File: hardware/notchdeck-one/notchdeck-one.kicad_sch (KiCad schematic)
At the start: 0 parts

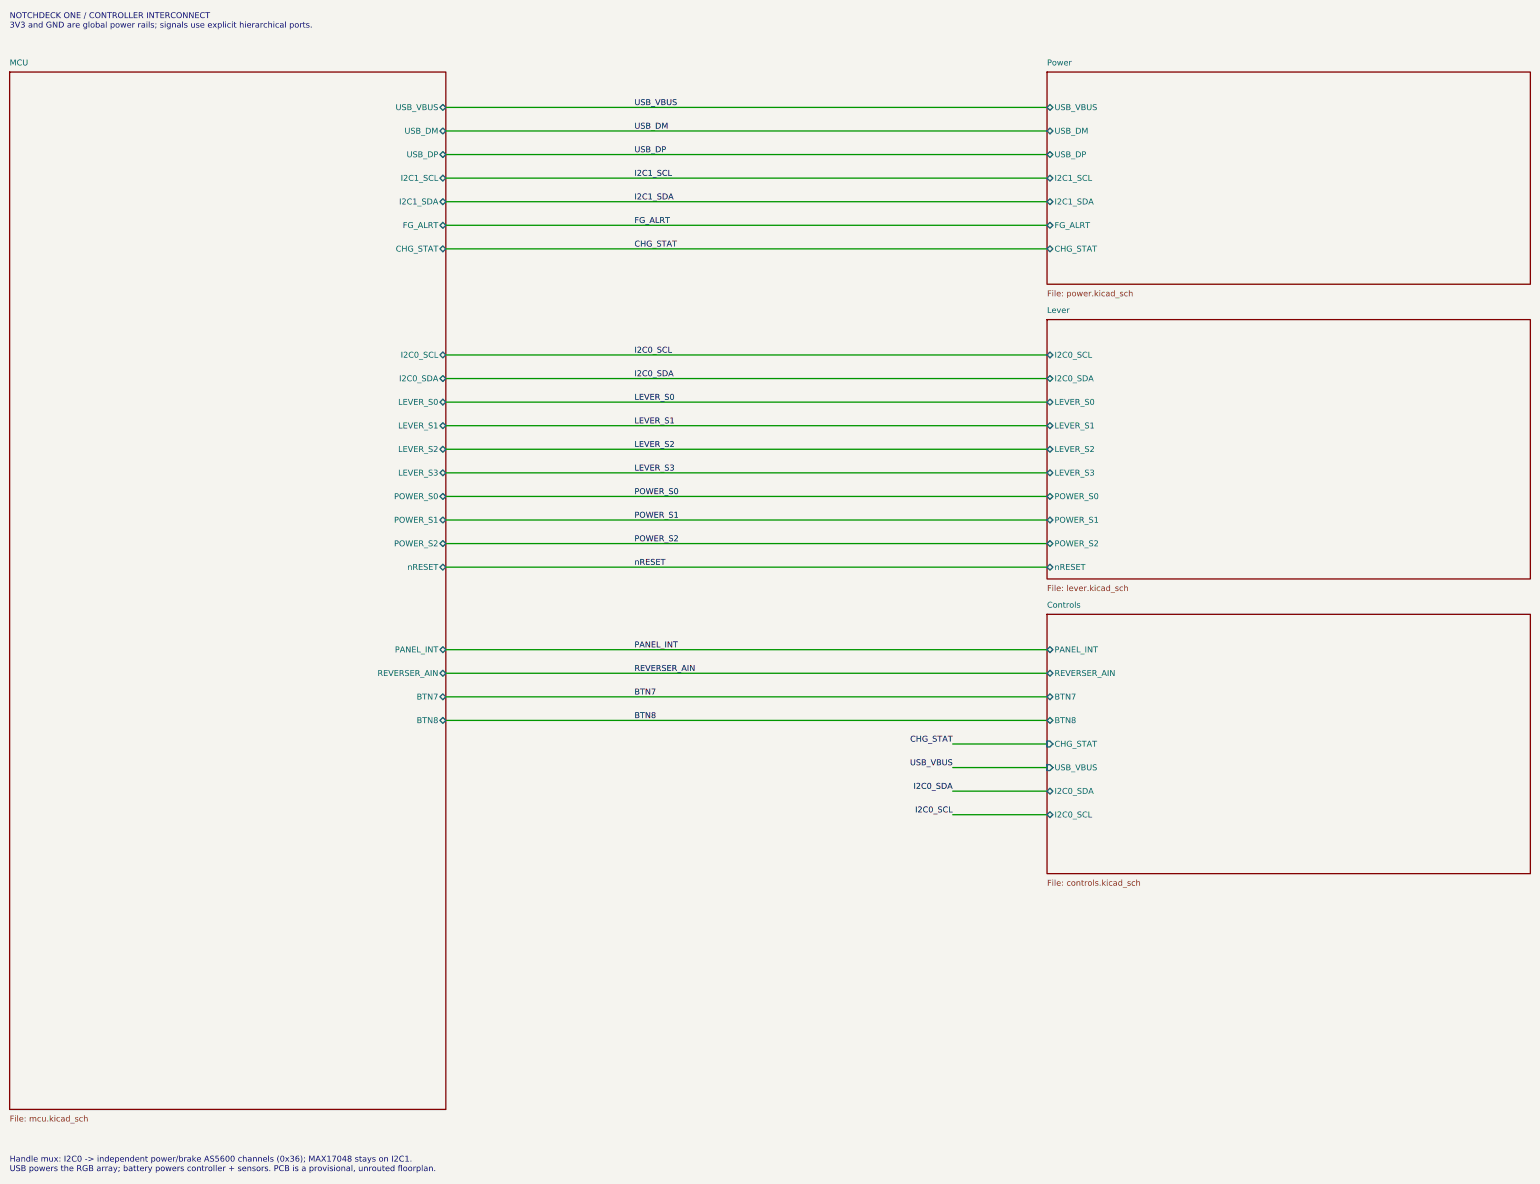
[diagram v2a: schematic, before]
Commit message: Add protected PWM actuator outputs and charger interlock
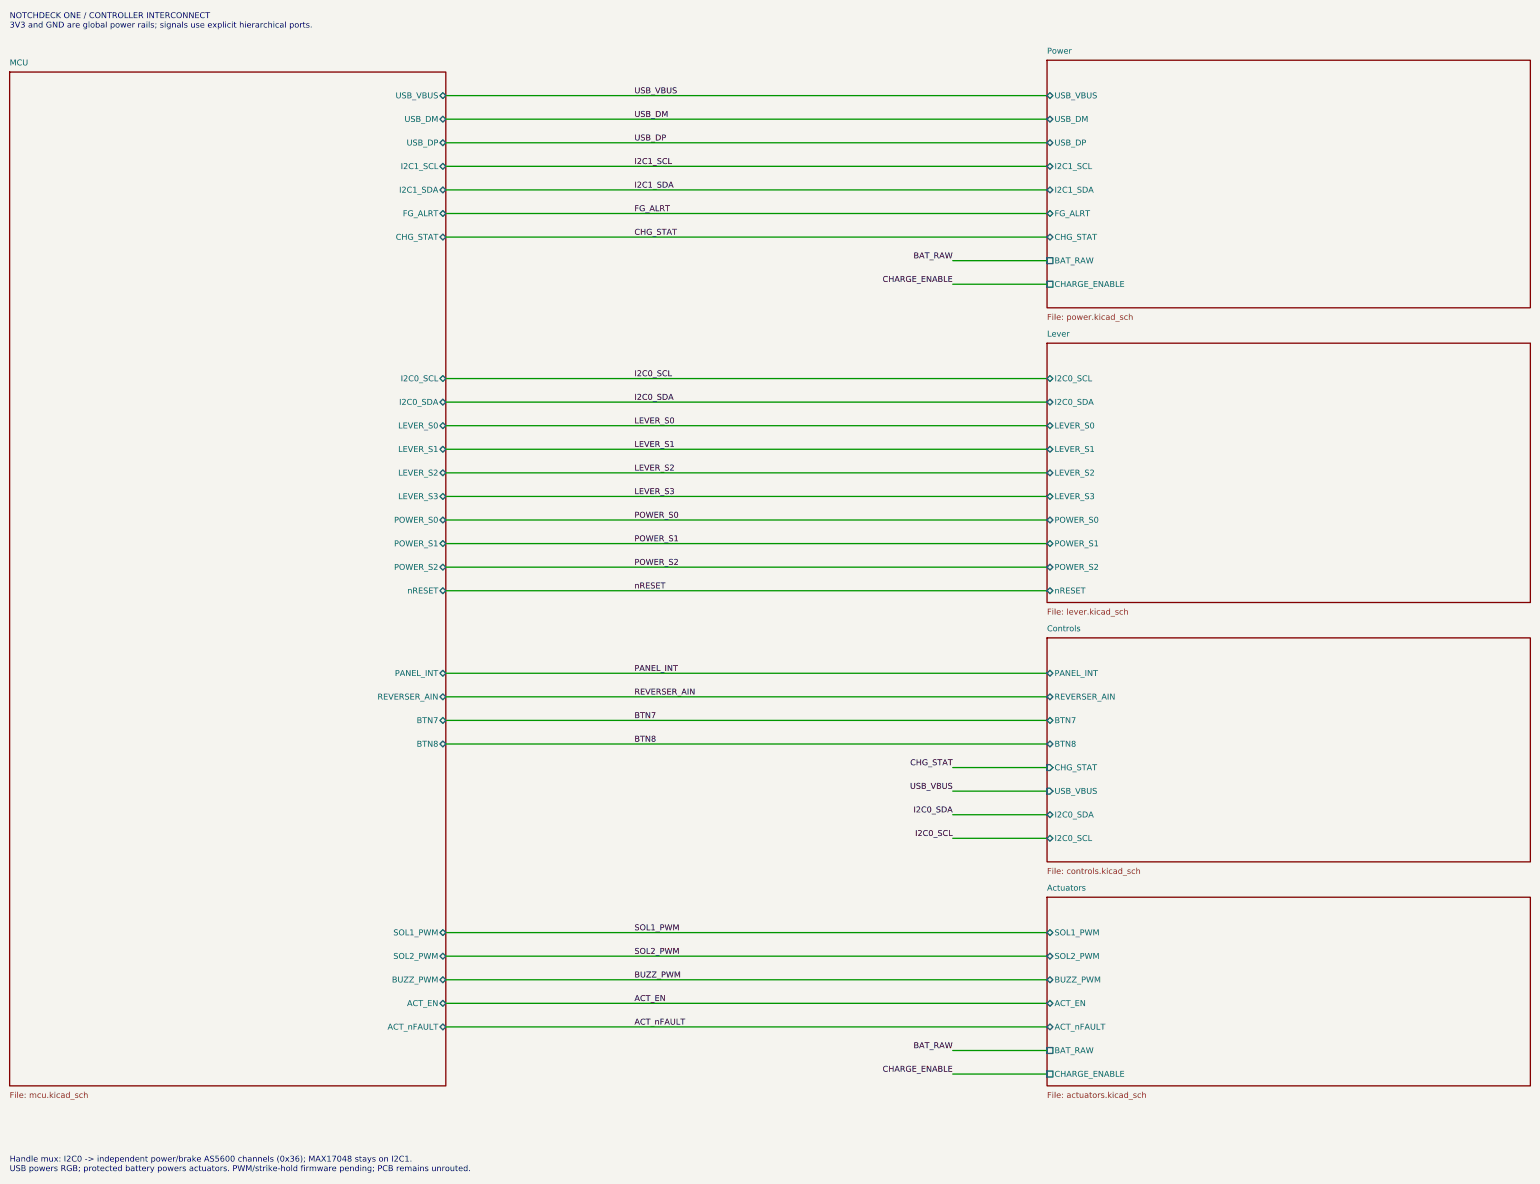
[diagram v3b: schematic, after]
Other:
- added sheet Actuators (actuators.kicad_sch)
- sheet MCU ports: added ACT_EN, ACT_nFAULT, BUZZ_PWM, SOL1_PWM, SOL2_PWM; removed none
- sheet Power ports: added BAT_RAW, CHARGE_ENABLE; removed none
- note added: "Handle mux: I2C0 -> independent power/brake AS5600 channels (0x36); MAX17048 stays on I2C1. USB powers RGB; protected battery powers actuators. PWM/strike-hold firmware pending; PCB remains unrouted."
- note removed: "Handle mux: I2C0 -> independent power/brake AS5600 channels (0x36); MAX17048 stays on I2C1. USB powers the RGB array; battery powers controller + sensors. PCB is a provisional, unrouted floorplan."

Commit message: Protect full battery input and size dual 2A impulse outputs
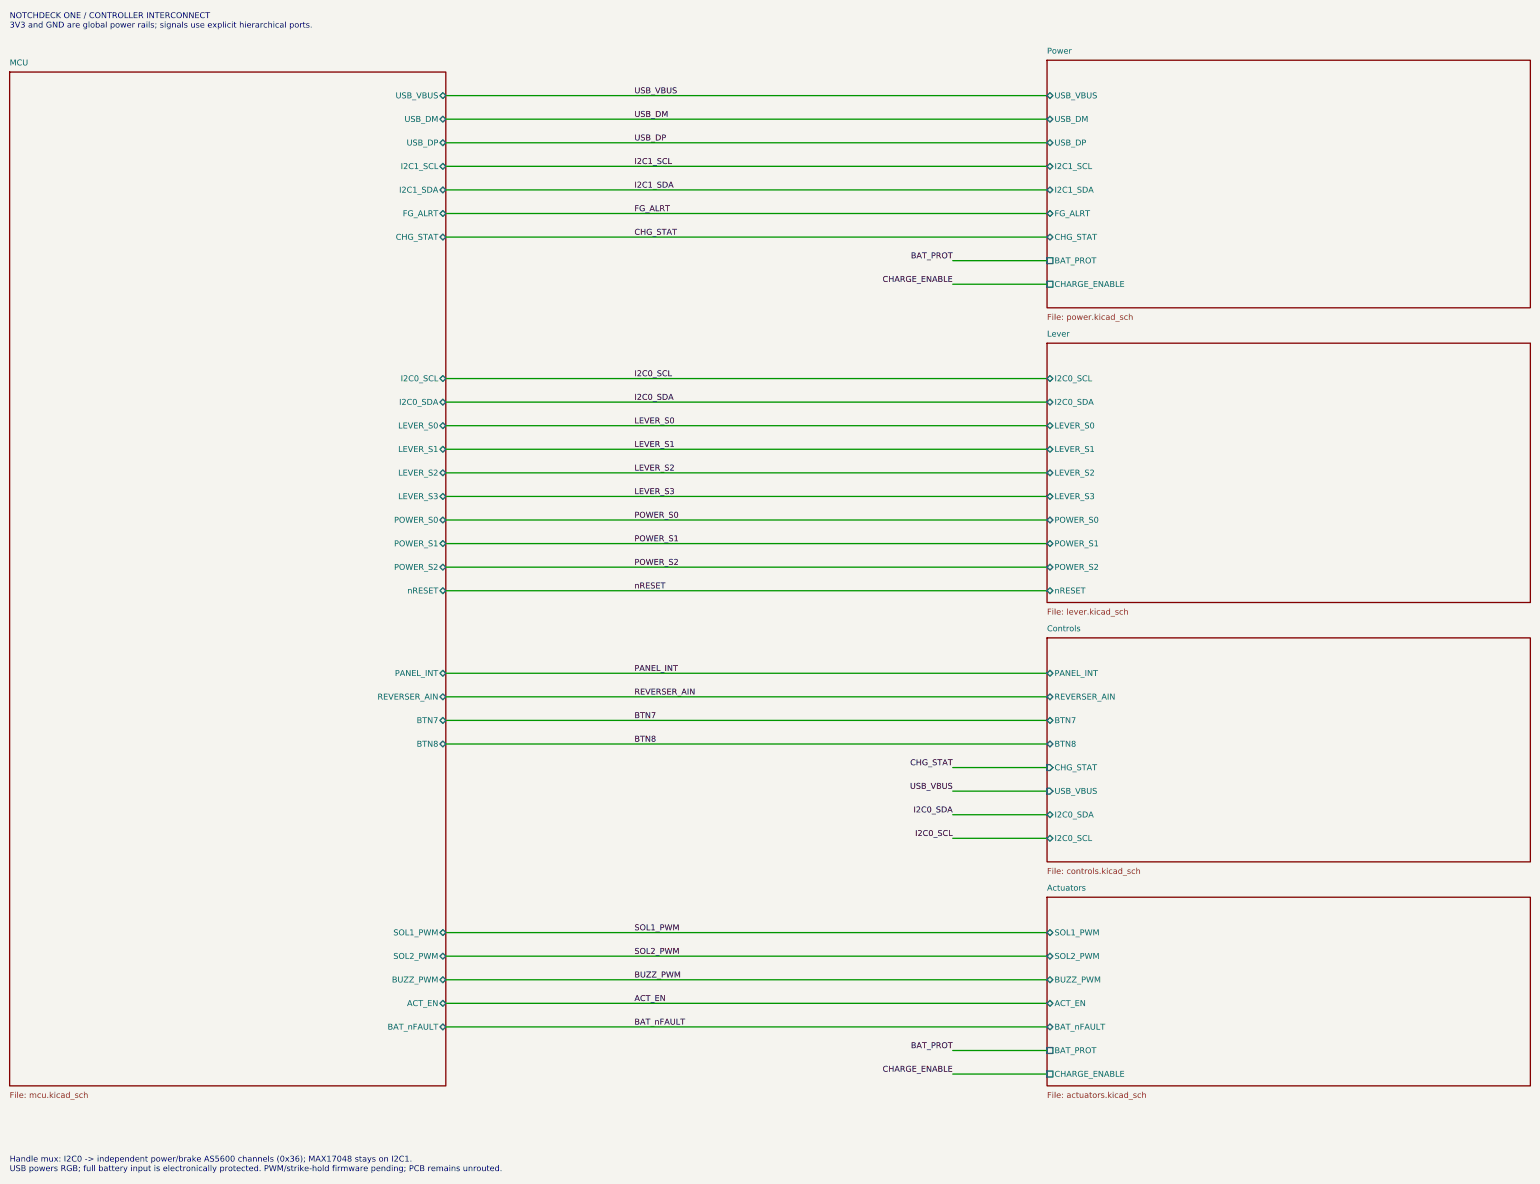
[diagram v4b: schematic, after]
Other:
- sheet Actuators ports: added BAT_PROT, BAT_nFAULT; removed ACT_nFAULT, BAT_RAW
- sheet MCU ports: added BAT_nFAULT; removed ACT_nFAULT
- sheet Power ports: added BAT_PROT; removed BAT_RAW
- note added: "Handle mux: I2C0 -> independent power/brake AS5600 channels (0x36); MAX17048 stays on I2C1. USB powers RGB; full battery input is electronically protected. PWM/strike-hold firmware pending; PCB remains unrouted."
- note removed: "Handle mux: I2C0 -> independent power/brake AS5600 channels (0x36); MAX17048 stays on I2C1. USB powers RGB; protected battery powers actuators. PWM/strike-hold firmware pending; PCB remains unrouted."
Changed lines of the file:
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@@
 		(title "NotchDeck One")
 		(date "2026-10-04")
-		(rev "F")
+		(rev "G")
 		(company "BenchBits")
 	)
@@
 			(effects (font (size 1.27 1.27)) (justify left))
 		)
-		(pin "BAT_RAW" passive
+		(pin "BAT_PROT" passive
 			(at 274.3200 71.1200 180)
 			(effects (font (size 1.27 1.27)) (justify left))
@@
 			(effects (font (size 1.27 1.27)) (justify left))
 		)
-		(pin "ACT_nFAULT" bidirectional
+		(pin "BAT_nFAULT" bidirectional
 			(at 274.3200 236.2200 180)
 			(effects (font (size 1.27 1.27)) (justify left))
 		)
-		(pin "BAT_RAW" passive
+		(pin "BAT_PROT" passive
 			(at 274.3200 241.3000 180)
 			(effects (font (size 1.27 1.27)) (justify left))
@@
 			(effects (font (size 1.27 1.27)) (justify right))
 		)
-		(pin "ACT_nFAULT" bidirectional
+		(pin "BAT_nFAULT" bidirectional
 			(at 144.7800 236.2200 0)
 			(effects (font (size 1.27 1.27)) (justify right))
@@
 		(stroke (width 0) (type default))
 	)
-	(label "BAT_RAW"
+	(label "BAT_PROT"
 		(at 254.0000 71.1200 180)
 		(effects (font (size 1.27 1.27)) (justify right bottom))
@@
 		(stroke (width 0) (type default))
 	)
-	(label "ACT_nFAULT"
+	(label "BAT_nFAULT"
 		(at 185.4200 236.2200 0)
 		(effects (font (size 1.27 1.27)) (justify left bottom))
@@
 		(stroke (width 0) (type default))
 	)
-	(label "BAT_RAW"
+	(label "BAT_PROT"
 		(at 254.0000 241.3000 180)
 		(effects (font (size 1.27 1.27)) (justify right bottom))
@@
 		(effects (font (face "Courier New") (size 1.27 1.27)) (justify left top))
 	)
-	(text "Handle mux: I2C0 -> independent power/brake AS5600 channels (0x36); MAX17048 stays on I2C1.\nUSB powers RGB; protected battery powers actuators. PWM/strike-hold firmware pending; PCB remains unrouted."
+	(text "Handle mux: I2C0 -> independent power/brake AS5600 channels (0x36); MAX17048 stays on I2C1.\nUSB powers RGB; full battery input is electronically protected. PWM/strike-hold firmware pending; PCB remains unrouted."
 		(exclude_from_sim no)
 		(at 50.80 264.16 0)
